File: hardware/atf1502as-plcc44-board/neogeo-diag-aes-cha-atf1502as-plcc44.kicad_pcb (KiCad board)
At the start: 2 copper layers, 173 x 134 mm, 20 parts, among them J1 neogeo-aes-cha-a-side-edge, J2 neogeo-aes-cha-a-side-edge, J3 neogeo-aes-cha-b-side-edge, J4 neogeo-aes-cha-b-side-edge, J5 JTAG, U1 74HC574, U2 ATF1502AS-xJx44, U3 74HC574, U4 27C010 / 27C1001, U5 27C010 / 27C1001

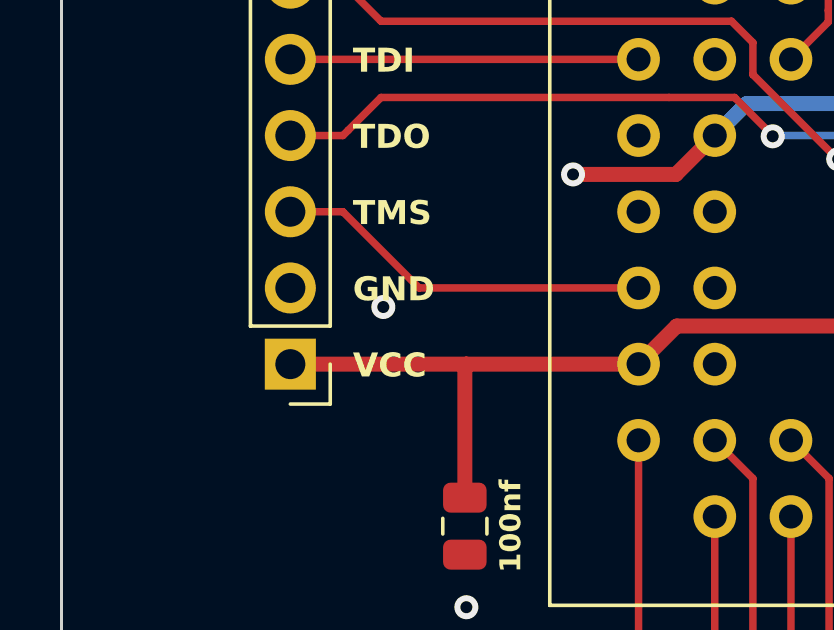
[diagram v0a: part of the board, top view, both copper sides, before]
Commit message: Minor tweaks, Bump revision number on all boards so they are the same
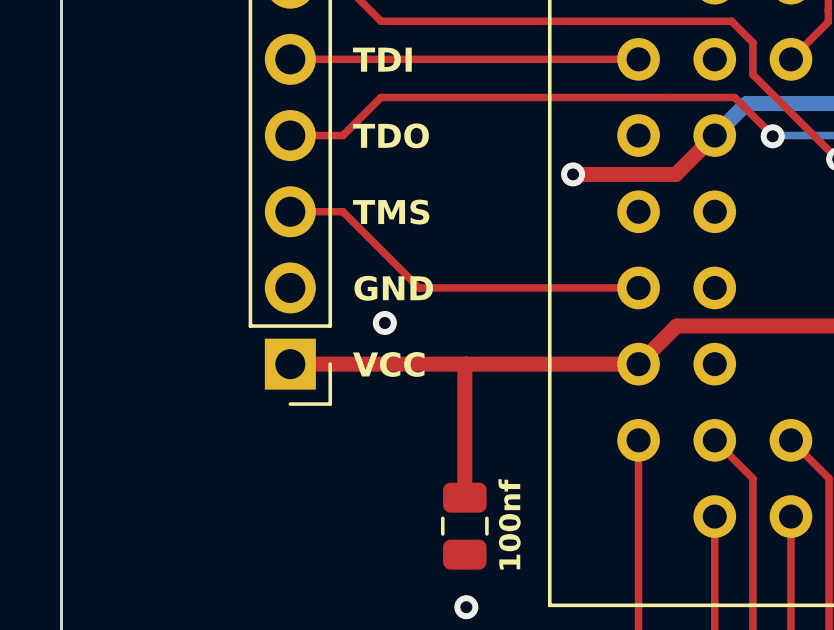
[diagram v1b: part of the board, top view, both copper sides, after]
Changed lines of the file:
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@@
     )
   )
-  (property "REV" "2023-07-30")
+  (property "REV" "2023-08-20")
   (net 0 "")
   (net 1 "VCC")
@@
   (via (at 226.06 55.88) (size 0.8) (drill 0.4) (layers "F.Cu" "B.Cu") (free) (net 2))
   (via (at 175.26 129.54) (size 0.8) (drill 0.4) (layers "F.Cu" "B.Cu") (free) (net 2))
-  (via (at 77.2668 94.996) (size 0.8) (drill 0.4) (layers "F.Cu" "B.Cu") (free) (net 2))
+  (via (at 77.3176 95.5294) (size 0.8) (drill 0.4) (layers "F.Cu" "B.Cu") (free) (net 2))
   (via (at 206.375 109.728) (size 0.8) (drill 0.4) (layers "F.Cu" "B.Cu") (free) (net 2))
   (via (at 154.94 74.93) (size 0.8) (drill 0.4) (layers "F.Cu" "B.Cu") (free) (net 2))
